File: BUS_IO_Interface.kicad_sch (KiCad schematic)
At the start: 41 parts, among them U12 MAX31331TETB+, U13 AS1016204-0108X0PWAY, U14 TCAN1044ADDFRQ1, U16 AS1016204-0108X0PWAY, U18 AS1016204-0108X0PWAY, U20 AS1016204-0108X0PWAY, U22 TCAN1044ADDFRQ1, Y3 32.768kHz

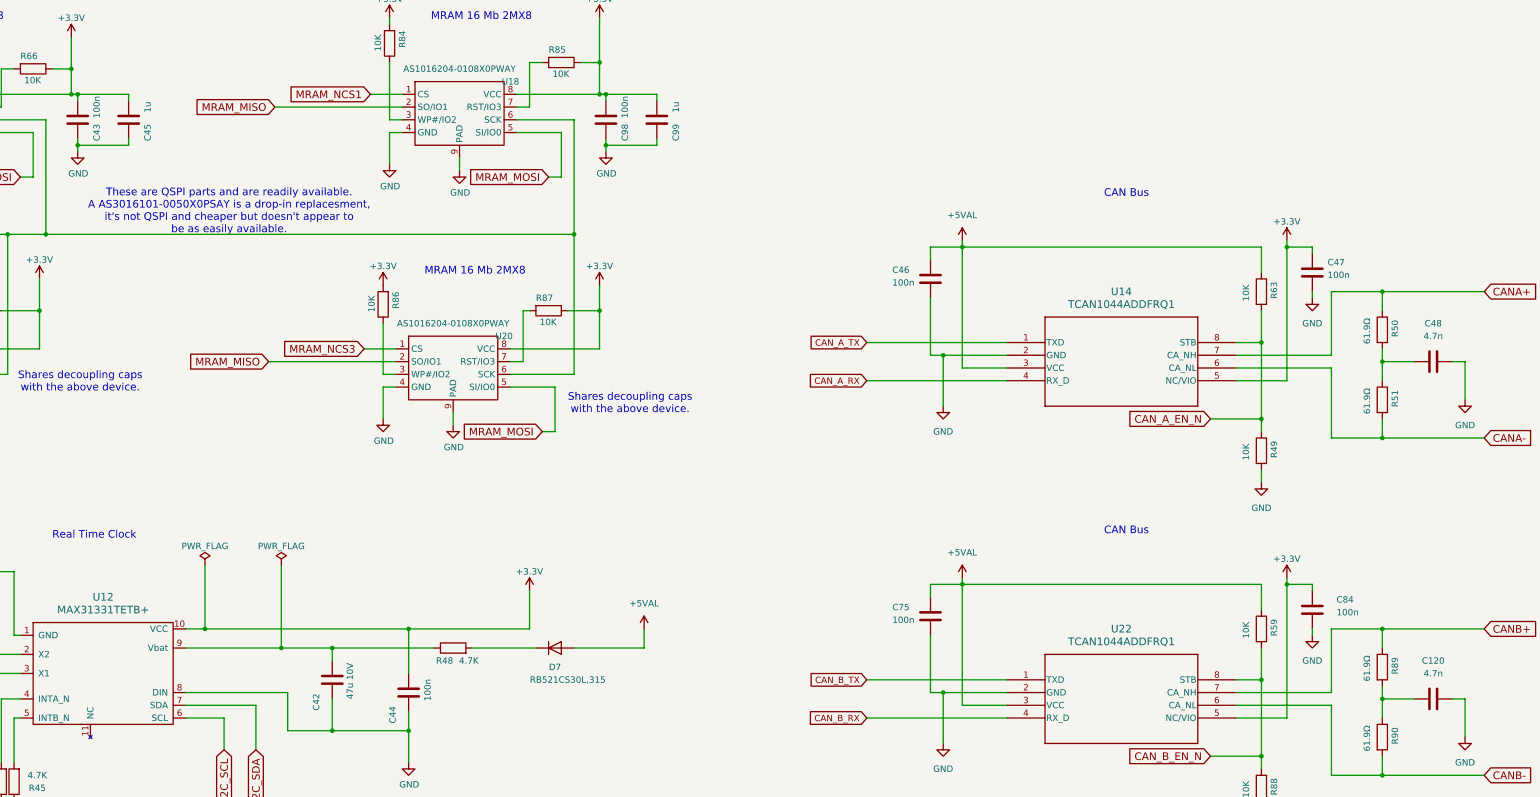
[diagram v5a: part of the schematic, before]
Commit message: Lots of updates to ease manufacturing
Component changes, changes in the formatting of the values, etc.

Signed-off-by: Corey Minyard <corey@minyard.net>
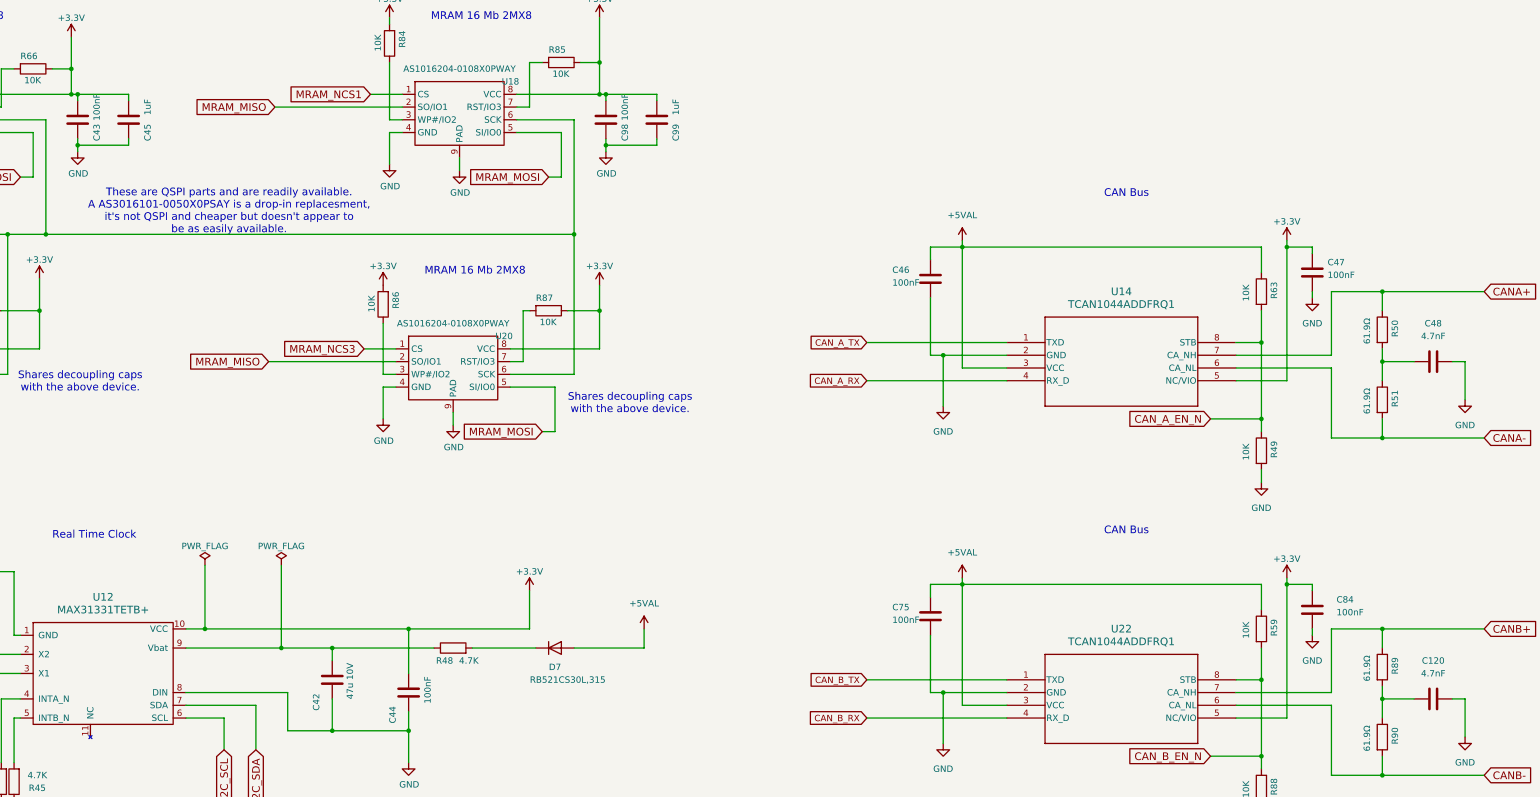
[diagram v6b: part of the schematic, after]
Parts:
- C120, C48: value 4.7n -> 4.7nF
- C43, C44, C46, C47, C75, C84, C98: value 100n -> 100nF
- C45, C99: value 1u -> 1uF
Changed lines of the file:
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@@
 			)
 		)
-		(property "Value" "100n"
+		(property "Value" "100nF"
 			(at 214.63 41.91 90)
 			(effects
@@
 			)
 		)
-		(property "Value" "100n"
+		(property "Value" "100nF"
 			(at 267.97 76.962 0)
 			(effects
@@
 			)
 		)
-		(property "Value" "100n"
+		(property "Value" "100nF"
 			(at 354.838 75.438 0)
 			(effects
@@
 			)
 		)
-		(property "Value" "100n"
+		(property "Value" "100nF"
 			(at 267.97 144.272 0)
 			(effects
@@
 			)
 		)
-		(property "Value" "4.7n"
+		(property "Value" "4.7nF"
 			(at 375.92 87.63 90)
 			(effects
@@
 			)
 		)
-		(property "Value" "4.7n"
+		(property "Value" "4.7nF"
 			(at 375.92 154.94 90)
 			(effects
@@
 			)
 		)
-		(property "Value" "100n"
+		(property "Value" "100nF"
 			(at 175.26 158.242 90)
 			(effects
@@
 			)
 		)
-		(property "Value" "1u"
+		(property "Value" "1uF"
 			(at 224.79 41.91 90)
 			(effects
@@
 			)
 		)
-		(property "Value" "100n"
+		(property "Value" "100nF"
 			(at 109.22 41.91 90)
 			(effects
@@
 			)
 		)
-		(property "Value" "1u"
+		(property "Value" "1uF"
 			(at 119.38 41.91 90)
 			(effects
@@
 			)
 		)
-		(property "Value" "100n"
+		(property "Value" "100nF"
 			(at 356.616 142.748 0)
 			(effects

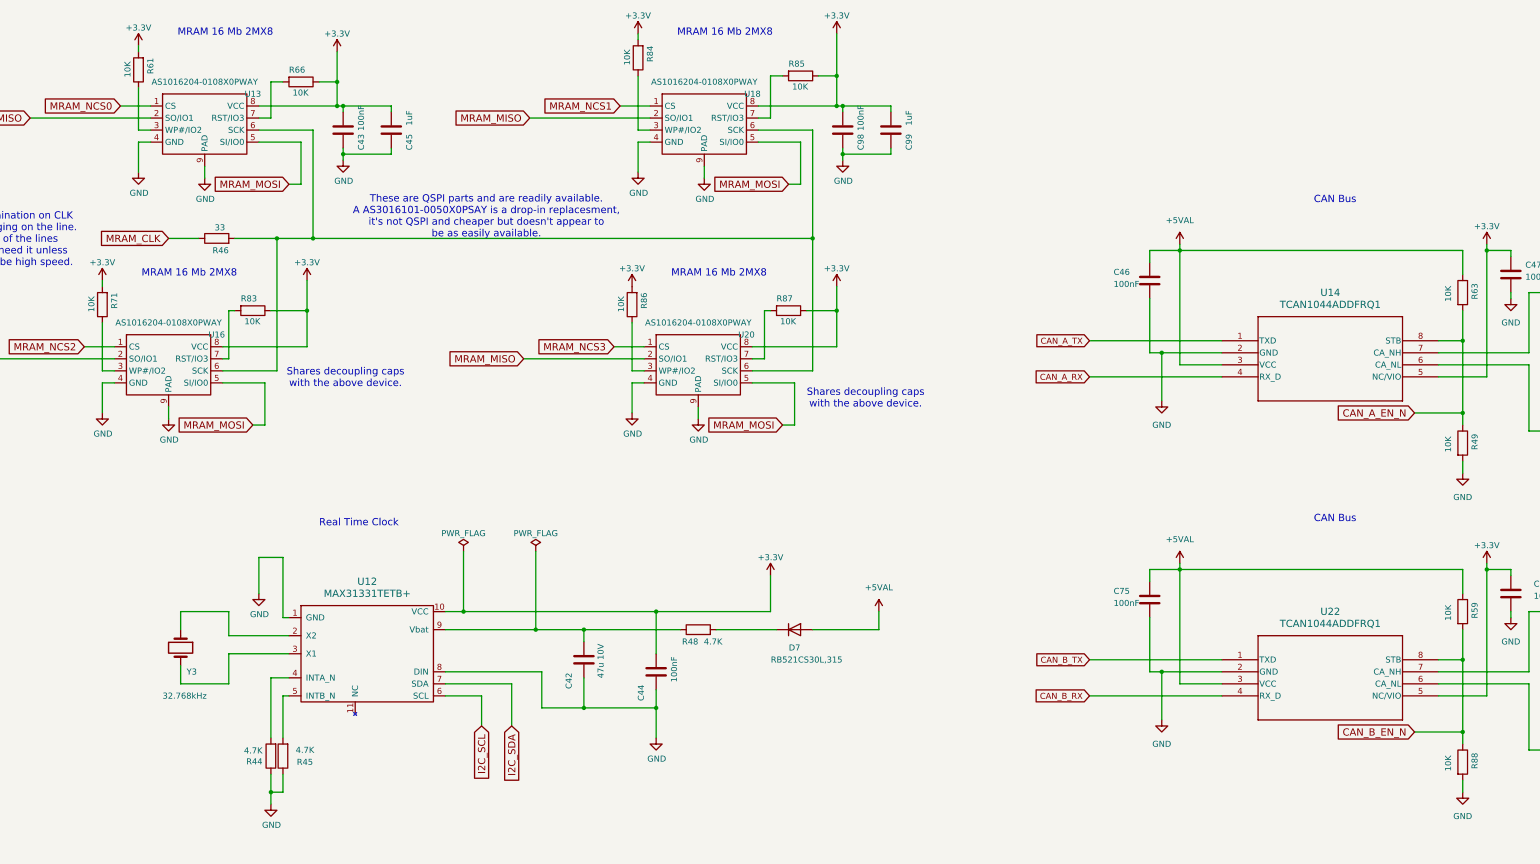
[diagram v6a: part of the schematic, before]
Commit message: Update all resistors to have an ohm symbol
Make it more clean in the BOM what they are.

Signed-off-by: Corey Minyard <corey@minyard.net>
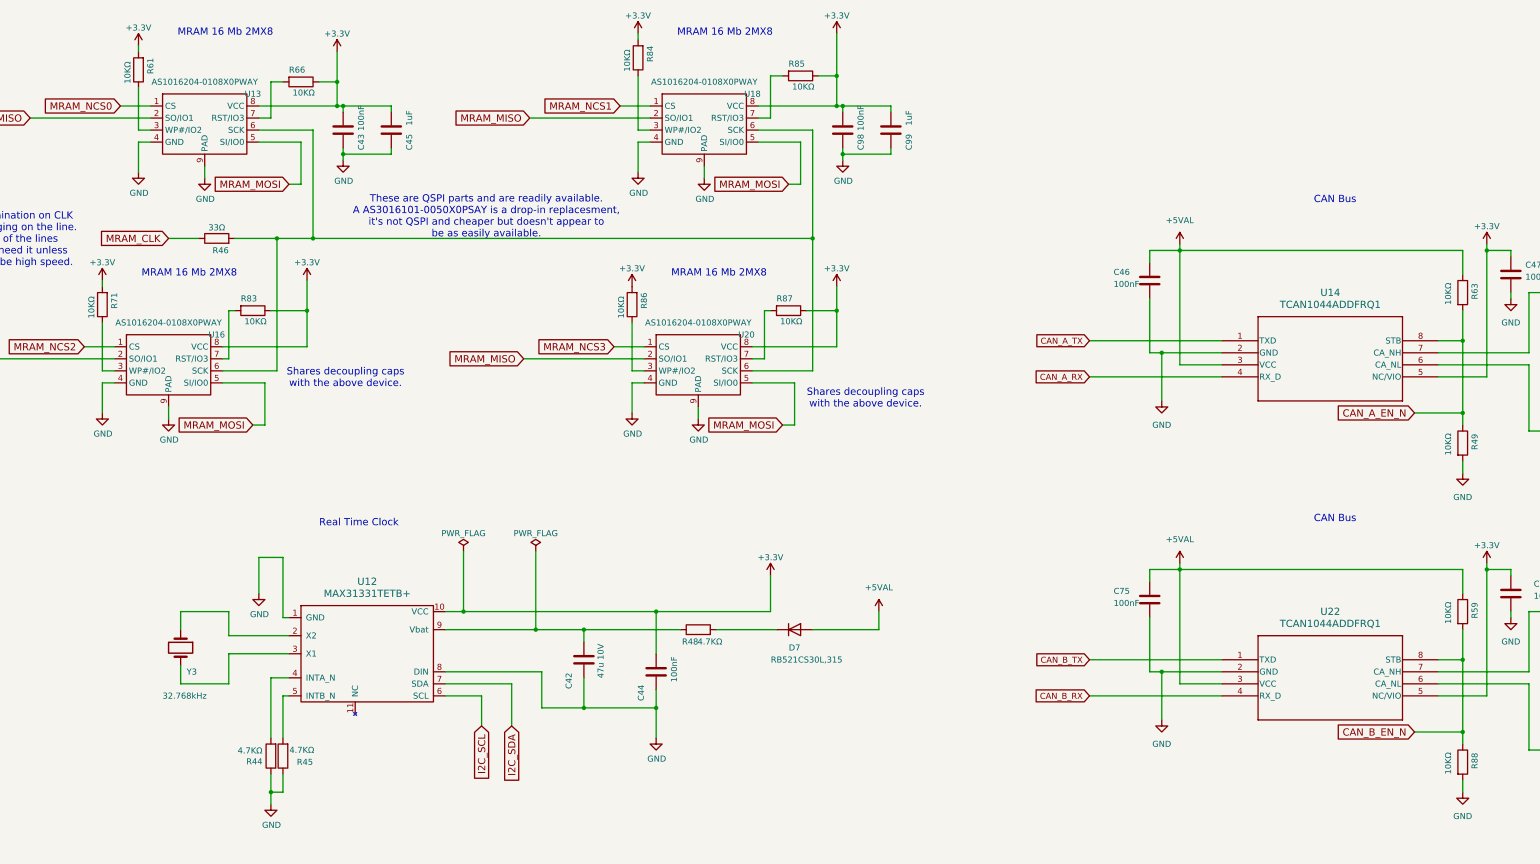
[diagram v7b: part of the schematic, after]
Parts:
- R44, R45, R48: value 4.7K -> 4.7KΩ
- R46: value 33 -> 33Ω
- R49, R59, R61, R63, R66, R71, R83, R84, R85, R86, R87, R88: value 10K -> 10KΩ
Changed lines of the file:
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@@
 			)
 		)
-		(property "Value" "4.7K"
+		(property "Value" "4.7KΩ"
 			(at 88.392 175.387 0)
 			(effects
@@
 			)
 		)
-		(property "Value" "10K"
+		(property "Value" "10KΩ"
 			(at 164.084 79.502 90)
 			(effects
@@
 			)
 		)
-		(property "Value" "10K"
+		(property "Value" "10KΩ"
 			(at 338.582 78.994 90)
 			(effects
@@
 			)
 		)
-		(property "Value" "33"
+		(property "Value" "33Ω"
 			(at 80.518 65.024 90)
 			(effects
@@
 			)
 		)
-		(property "Value" "10K"
+		(property "Value" "10KΩ"
 			(at 338.582 146.304 90)
 			(effects
@@
 			)
 		)
-		(property "Value" "10K"
+		(property "Value" "10KΩ"
 			(at 52.324 79.502 90)
 			(effects
@@
 			)
 		)
-		(property "Value" "10K"
+		(property "Value" "10KΩ"
 			(at 197.612 84.836 90)
 			(effects
@@
 			)
 		)
-		(property "Value" "10K"
+		(property "Value" "10KΩ"
 			(at 200.152 35.306 90)
 			(effects
@@
 			)
 		)
-		(property "Value" "10K"
+		(property "Value" "10KΩ"
 			(at 165.354 27.432 90)
 			(effects
@@
 			)
 		)
-		(property "Value" "10K"
+		(property "Value" "10KΩ"
 			(at 59.944 29.972 90)
 			(effects
@@
 			)
 		)
-		(property "Value" "10K"
+		(property "Value" "10KΩ"
 			(at 94.742 36.576 90)
 			(effects
@@
 			)
 		)
-		(property "Value" "4.7K"
+		(property "Value" "4.7KΩ"
 			(at 185.42 152.4 90)
 			(effects
@@
 			)
 		)
-		(property "Value" "4.7K"
+		(property "Value" "4.7KΩ"
 			(at 99.314 175.26 0)
 			(effects
@@
 			)
 		)
-		(property "Value" "10K"
+		(property "Value" "10KΩ"
 			(at 338.582 178.054 90)
 			(effects
@@
 			)
 		)
-		(property "Value" "10K"
+		(property "Value" "10KΩ"
 			(at 84.582 84.836 90)
 			(effects
@@
 			)
 		)
-		(property "Value" "10K"
+		(property "Value" "10KΩ"
 			(at 338.582 110.744 90)
 			(effects

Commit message: Finish up temporary PC104 assignments
Finish up most of what is required for the CubeSat Kit Bus conversion.

Signed-off-by: Corey Minyard <corey@minyard.net>
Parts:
- U14, U22: footprint Package_TO_SOT_SMD:TSOT-23-8 -> PacSatDev_misc:TSOT-23-8
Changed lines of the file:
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@@
 			)
 		)
-		(property "Footprint" "Package_TO_SOT_SMD:TSOT-23-8"
+		(property "Footprint" "PacSatDev_misc:TSOT-23-8"
 			(at 290.83 156.21 0)
 			(effects
@@
 			)
 		)
-		(property "Footprint" "Package_TO_SOT_SMD:TSOT-23-8"
+		(property "Footprint" "PacSatDev_misc:TSOT-23-8"
 			(at 290.83 88.9 0)
 			(effects
